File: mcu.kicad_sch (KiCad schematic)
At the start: 4 parts, among them U3 ADAFRUIT_QT_PY

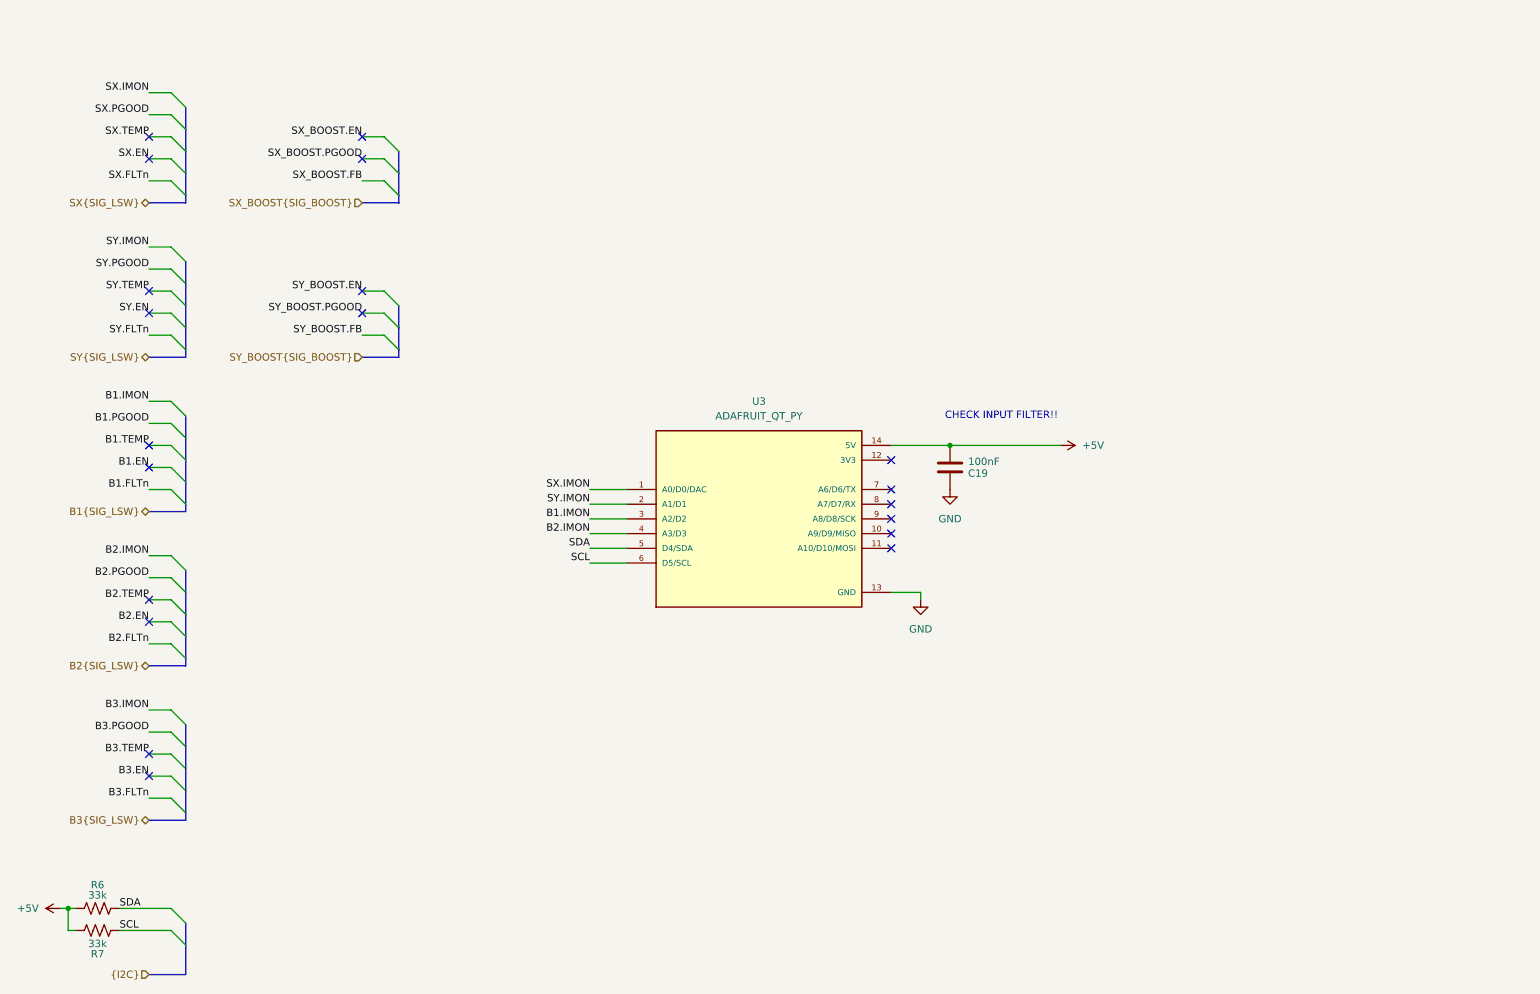
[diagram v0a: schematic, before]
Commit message: imu and load switch for navlight
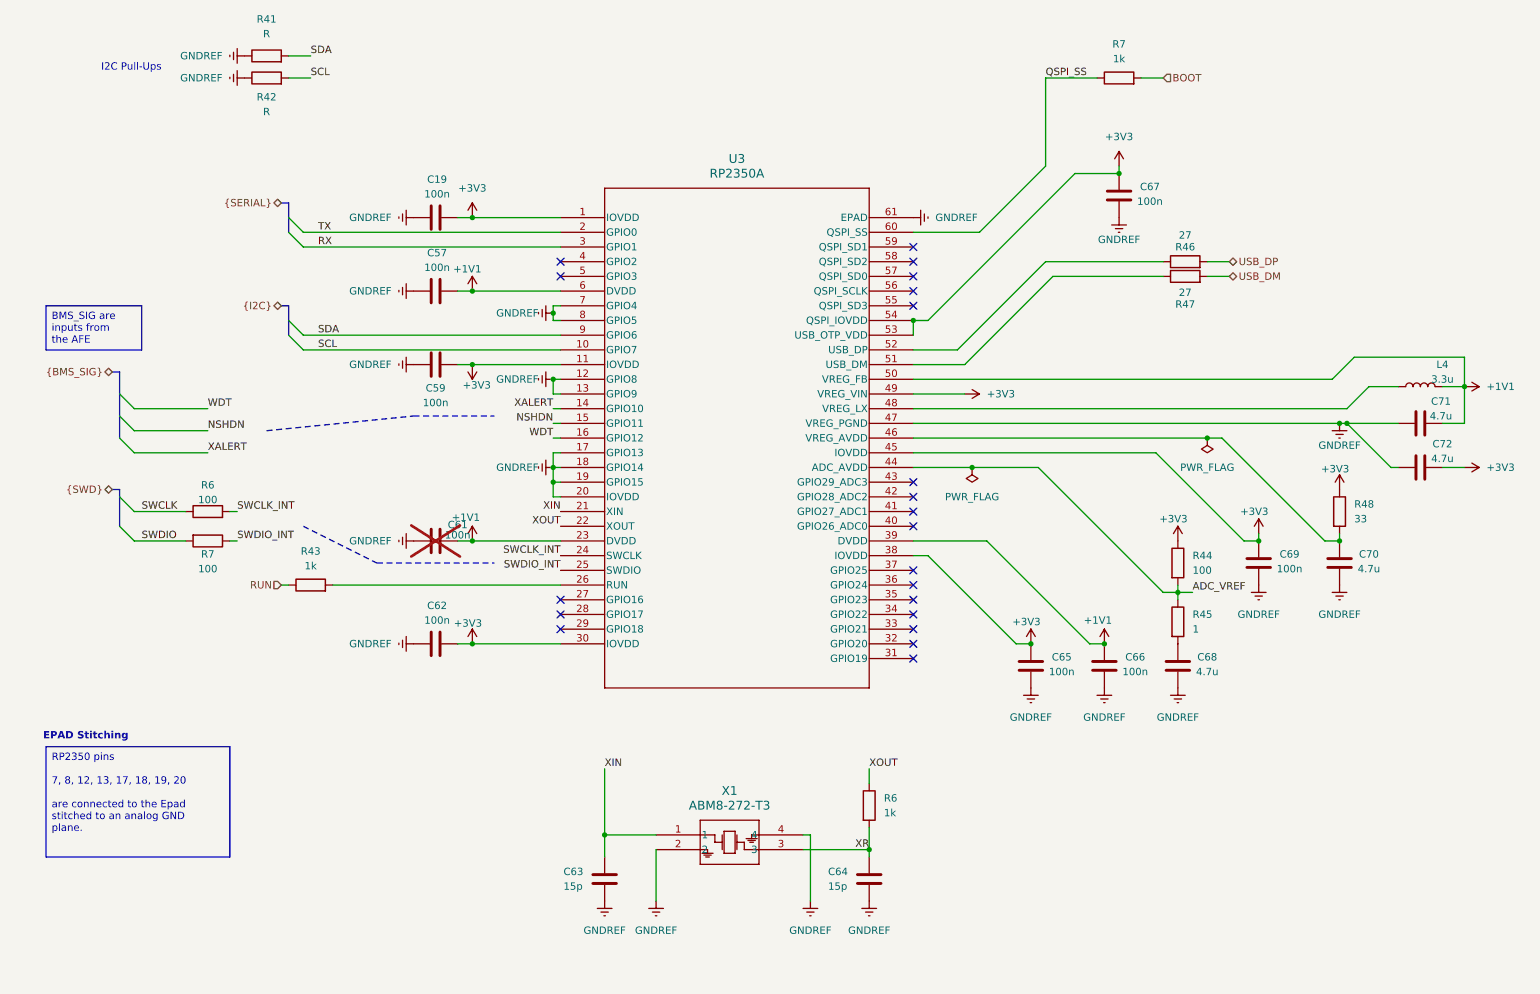
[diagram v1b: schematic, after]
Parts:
- removed R6, R7: 33k, Resistor_SMD:R_0603_1608Metric, symbol Device:R_US
- removed U3: ADAFRUIT_QT_PY, _Power_Board:MODULE_ADAFRUIT_QT_PY, symbol _RP2040:ADAFRUIT_QT_PY
- added C57, C59, C61, C62, C65, C66, C67, C69: 100n, Capacitor_SMD:C_0201_0603Metric, symbol Device:C
- added C63, C64: 15p, Resistor_SMD:R_0201_0603Metric, symbol Device:C
- added C68, C70, C71, C72: 4.7u, Capacitor_SMD:C_0402_1005Metric, symbol Device:C
- added L4: 3.3u, Inductor_SMD:L_0805_2012Metric, symbol Device:L
- added R41, R42: R, symbol Device:R
- added R43, R7: 1k, Resistor_SMD:R_0402_1005Metric, symbol Device:R
- added R44: 100, Capacitor_SMD:C_0402_1005Metric, symbol Device:R
- added R45: 1, Resistor_SMD:R_0402_1005Metric, symbol Device:R
- added R46, R47: 27, Resistor_SMD:R_0201_0603Metric, symbol Device:R
- added R48: 33, Resistor_SMD:R_0402_1005Metric, symbol Device:R
- added R6, R7: 100, Resistor_SMD:R_0201_0603Metric, symbol Device:R
- added R6: 1k, Resistor_SMD:R_0201_0603Metric, symbol Device:R
- added U3: RP2350A, _BMS:QFN-60_7X7_RPI, symbol _RP2354A:RP2350A
- added X1: ABM8-272-T3, _BMS:ABM8-272-T3_ABR, symbol _AMB8:ABM8-272-T3
- C19: value 100nF -> 100n; footprint Capacitor_SMD:C_1206_3216Metric -> Capacitor_SMD:C_0201_0603Metric; Mfr P/N GCM31C5C1H104FA16L -> GRT033R60J104KE01D; Supplier_1 P/N 490-GCM31C5C1H104FA16LTR-ND -> 490-16306-2-ND; Supplier_1 Unit Price 0.98000 -> 0.10000
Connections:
- net SCL: now also R42.2, U3.10 (GPIO7)
- net SDA: now also R41.2, U3.9 (GPIO6)
- net +5V renamed GNDREF
- net GNDREF: now also C57.1, C59.1, C61.1, C62.1, C63.2, C64.2, C65.2, C66.2, C67.2, C68.2, C69.2, C70.2, C71.1, C72.1, R41.1, R42.1, U3.12 (GPIO8), U3.13 (GPIO9), U3.17 (GPIO13), U3.18 (GPIO14), U3.19 (GPIO15), U3.20 (IOVDD), U3.47 (VREG_PGND), U3.61 (EPAD), U3.7 (GPIO4), U3.8 (GPIO5), X1.2, X1.4
- net GND renamed +3V3
- net +3V3: now also C59.2, C62.2, C65.1, C67.1, C69.1, C72.2, R44.1, R48.1, U3.1 (IOVDD), U3.11 (IOVDD), U3.30 (IOVDD), U3.38 (IOVDD), U3.45 (IOVDD), U3.49 (VREG_VIN), U3.53 (USB_OTP_VDD), U3.54 (QSPI_IOVDD)
- new net: L4.1, U3.48 (VREG_LX)
- new net: C68.1, R45.2
- new net: R43.2, U3.26 (RUN)
- new net: C70.1, R48.2, U3.46 (VREG_AVDD)
- new net: R47.1, U3.51 (USB_DM)
- new net: R46.1, U3.52 (USB_DP)
- new net +1V1: C57.2, C61.2, C66.1, C71.2, L4.2, U3.23 (DVDD), U3.39 (DVDD), U3.50 (VREG_FB), U3.6 (DVDD)
- new net ADC_VREF: R44.2, R45.1, U3.44 (ADC_AVDD)
- new net BOOT: R7.2
- new net NSHDN: U3.15 (GPIO11)
- new net QSPI_SS: R7.1, U3.60 (QSPI_SS)
- new net RUN: R43.1
- new net RX: U3.3 (GPIO1)
- new net SWCLK: R6.1
- new net SWCLK_INT: R6.2, U3.24 (SWCLK)
- new net SWDIO: R7.2
- new net SWDIO_INT: R7.1, U3.25 (SWDIO)
- new net TX: U3.2 (GPIO0)
- new net USB_DM: R47.2
- new net USB_DP: R46.2
- new net WDT: U3.16 (GPIO12)
- new net XALERT: U3.14 (GPIO10)
- new net XIN: C63.1, U3.21 (XIN), X1.1
- new net XOUT: R6.1, U3.22 (XOUT)
- new net XR: C64.1, R6.2, X1.3
- no-connect marks 20 -> 21
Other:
- note added: "EPAD Stitching"
- note added: "I2C Pull-Ups"
- note removed: "CHECK INPUT FILTER!!"
- title: House keeping -> IMU

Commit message: PowerBoard update with LVBUS
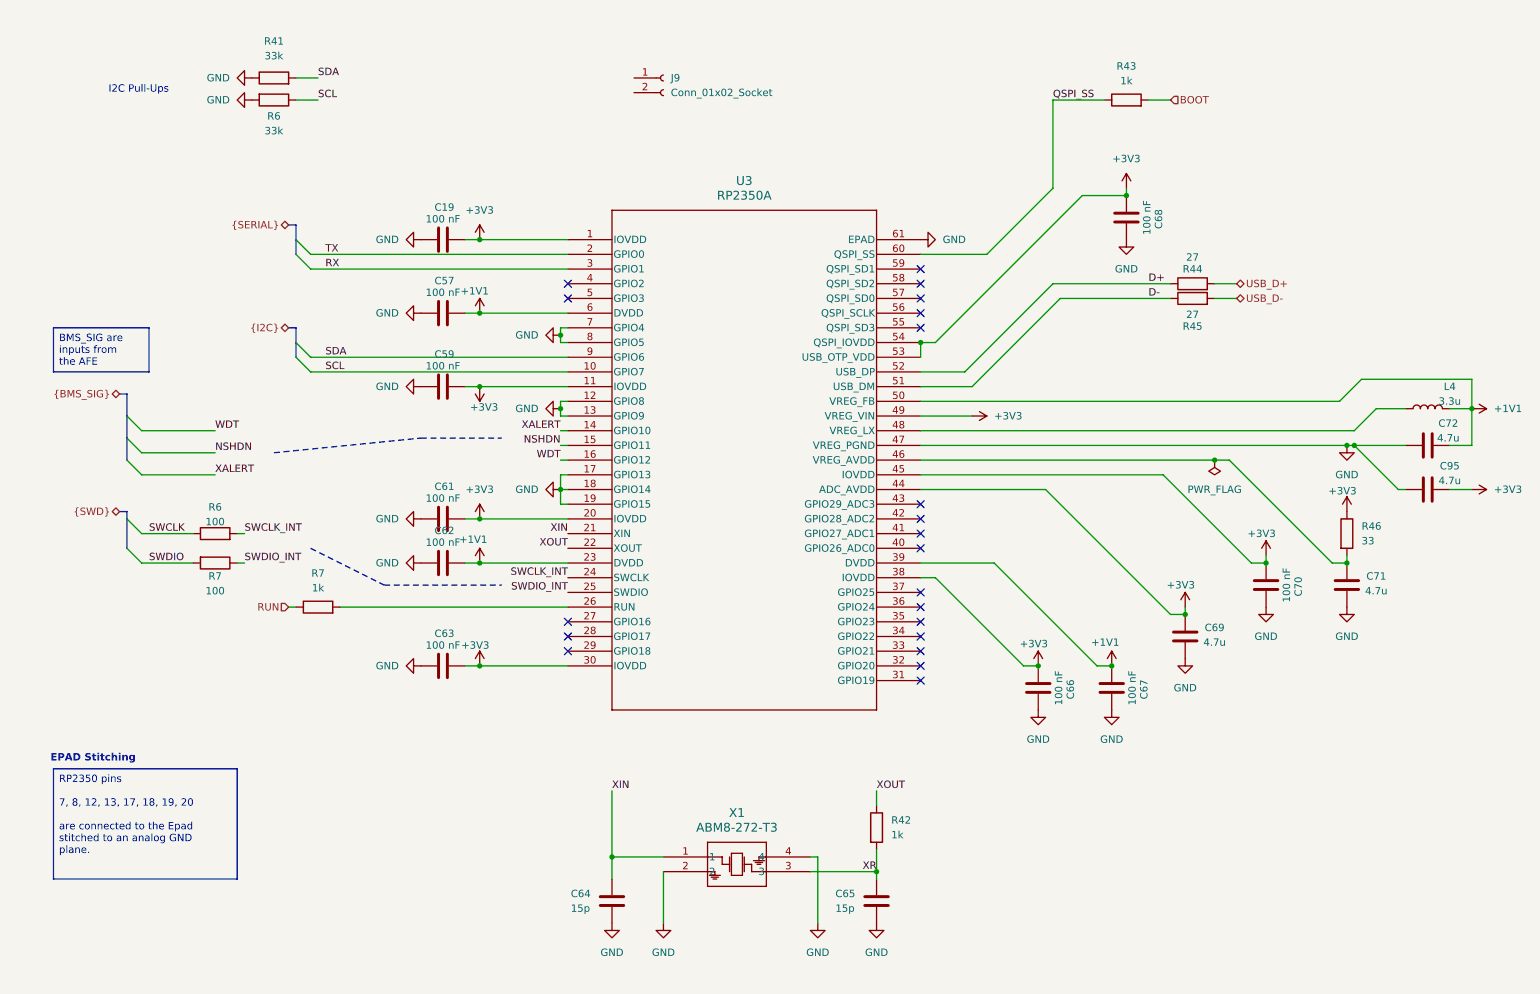
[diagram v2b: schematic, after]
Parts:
- removed R47: 27, Resistor_SMD:R_0201_0603Metric, symbol Device:R
- removed R48: 33, Resistor_SMD:R_0402_1005Metric, symbol Device:R
- removed R6, R7: 100, Resistor_SMD:R_0201_0603Metric, symbol Device:R
- removed R6: 1k, Resistor_SMD:R_0201_0603Metric, symbol Device:R
- removed R7: 1k, Resistor_SMD:R_0402_1005Metric, symbol Device:R
- added C95: 4.7u, Capacitor_SMD:C_0402_1005Metric, symbol Device:C
- added J9: Conn_01x02_Socket, Connector_JST:JST_PH_B2B-PH-K_1x02_P2.00mm_Vertical, symbol Connector:Conn_01x02_Socket
- added R6, R7: 100, Resistor_SMD:R_0201_0603Metric, symbol Device:R
- added R6: 33k, Resistor_SMD:R_0402_1005Metric, symbol Device:R
- added R7: 1k, Resistor_SMD:R_0402_1005Metric, symbol Device:R
- C19, C57, C59, C62, C66, C67: value 100n -> 100 nF; footprint Capacitor_SMD:C_0201_0603Metric -> Capacitor_SMD:C_0402_1005Metric; Mfr P/N GRT033R60J104KE01D -> GRM155C71H104JE19D; Supplier_1 Digikey -> DigiKey; Supplier_1 P/N 490-16306-2-ND -> 490-GRM155C71H104JE19DTR-ND; Supplier_1 Price @ QTY (none) -> 1; Supplier_1 Price @ Qty 1 -> (none)
- C61: value 100n -> 100 nF; footprint Capacitor_SMD:C_0201_0603Metric -> Capacitor_SMD:C_0402_1005Metric; Mfr P/N GRT033R60J104KE01D -> GRM155C71H104JE19D; Supplier_1 Digikey -> DigiKey; Supplier_1 P/N 490-16306-2-ND -> 490-GRM155C71H104JE19DTR-ND; Supplier_1 Price @ QTY (none) -> 1; Supplier_1 Price @ Qty 1 -> (none); now fitted; now in the parts list
- C63: value 15p -> 100 nF; footprint Resistor_SMD:R_0201_0603Metric -> Capacitor_SMD:C_0402_1005Metric; Mfr P/N GRM0335C1E150JA01D -> GRM155C71H104JE19D; Supplier_1 Digikey -> DigiKey; Supplier_1 P/N 490-9658-2-ND -> 490-GRM155C71H104JE19DTR-ND; Supplier_1 Price @ QTY (none) -> 1; Supplier_1 Price @ Qty 1 -> (none)
- C65: value 100n -> 15p; footprint Capacitor_SMD:C_0201_0603Metric -> Resistor_SMD:R_0201_0603Metric; Mfr P/N GRT033R60J104KE01D -> GRM0335C1E150JA01D; Supplier_1 P/N 490-16306-2-ND -> 490-9658-2-ND
- C68, C70: value 4.7u -> 100 nF; Mfr P/N GRM155R60J475ME87D -> GRM155C71H104JE19D; Supplier_1 Digkey -> DigiKey; Supplier_1 P/N 490-5408-2-ND -> 490-GRM155C71H104JE19DTR-ND; Supplier_1 Price @ QTY (none) -> 1; Supplier_1 Price @ Qty 1 -> (none)
- C69: value 100n -> 4.7u; footprint Capacitor_SMD:C_0201_0603Metric -> Capacitor_SMD:C_0402_1005Metric; Mfr P/N GRT033R60J104KE01D -> GRM155R60J475ME87D; Supplier_1 Digikey -> Digkey; Supplier_1 P/N 490-16306-2-ND -> 490-5408-2-ND
- R41: value R -> 33k; footprint (none) -> Resistor_SMD:R_0402_1005Metric; Mfr (none) -> KOA Speer Electronics, Inc.; Mfr P/N (none) -> RN73R1ETTP3302B25; Supplier_1 (none) -> Digikey; Supplier_1 P/N (none) -> 2019-RN73R1ETTP3302B25TR-ND; Supplier_1 Price @ Qty (none) -> 1; Supplier_1 Unit Price (none) -> 0.10000
- R42: value R -> 1k; footprint (none) -> Resistor_SMD:R_0201_0603Metric; Mfr (none) -> Bourns Inc.; Mfr P/N (none) -> CR0201AFW-1001GAS; Supplier_1 (none) -> Digikey; Supplier_1 P/N (none) -> CR0201AFW-1001GASTR-ND; Supplier_1 Price @ Qty (none) -> 1; Supplier_1 Unit Price (none) -> 0.1
- R44: value 100 -> 27; footprint Capacitor_SMD:C_0402_1005Metric -> Resistor_SMD:R_0201_0603Metric; Mfr P/N RC0402FR-07100RL -> RC0201FR-0727RL; Supplier_1 P/N 311-100LRTR-ND -> YAG2554TR-ND
- R45: value 1 -> 27; footprint Resistor_SMD:R_0402_1005Metric -> Resistor_SMD:R_0201_0603Metric; Mfr Stackpole Electronics Inc -> YAGEO; Mfr P/N RMCF0402FT1R00 -> RC0201FR-0727RL; Supplier_1 P/N 738-RMCF0402FT1R00TR-ND -> YAG2554TR-ND
- R46: value 27 -> 33; footprint Resistor_SMD:R_0201_0603Metric -> Resistor_SMD:R_0402_1005Metric; Mfr YAGEO -> Vishay Dale; Mfr P/N RC0201FR-0727RL -> TNPW040233R0DEED; Supplier_1 P/N YAG2554TR-ND -> 541-TNPW040233R0DEEDTR-ND; Supplier_1 Unit Price 0.10000 -> 0.20000
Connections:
- net USB_DP is gone; now on an unnamed net: R46.2
- net +1V1: now also C57.1, C62.1, C67.2, C72.2; no longer C57.2, C61.2, C66.1, C71.2
- net +3V3: now also C19.1, C59.1, C61.1, C63.1, C66.2, C68.2, C70.2, R46.1, U3.20 (IOVDD), U3.44 (ADC_AVDD), C95.2; no longer C19.2, C59.2, C62.2, C65.1, C67.1, C72.2, R44.1
- net BOOT: now also R43.2
- net QSPI_SS: now also R43.1
- net RUN: now also R7.1; no longer R43.1
- net SCL: now also R6.1; no longer R42.2
- net SWCLK: now also R6.1
- net SWCLK_INT: now also R6.2
- net SWDIO: now also R7.2
- net SWDIO_INT: now also R7.1
- net XIN: now also C64.1; no longer C63.1
- net XOUT: now also R42.1
- net XR: now also C65.1, R42.2; no longer C64.1
- net GND: now reaches C68.1
- net GND: now also C19.2, C57.2, C59.2, C61.2, C62.2, C63.2, C64.2, C65.2, C66.1, C67.1, C69.2, C70.1, C71.2, C72.1, R41.1, U3.12 (GPIO8), U3.13 (GPIO9), U3.17 (GPIO13), U3.18 (GPIO14), U3.19 (GPIO15), U3.47 (VREG_PGND), U3.61 (EPAD), U3.7 (GPIO4), U3.8 (GPIO5), X1.2, X1.4, C95.1, R6.2; no longer R45.2
- net at U3.26 (RUN): now also R7.2; no longer R43.2
- net at U3.46 (VREG_AVDD): now also C71.1; no longer C70.1
- net D-: now reaches U3.51 (USB_DM)
- net D-: now also R45.1
- net D+: now reaches U3.52 (USB_DP)
- net D+: now also R44.1; no longer R46.1
- removed net ADC_VREF: R44.2, R45.1, U3.44 (ADC_AVDD)
- removed net GNDREF: C19.1, C57.1, C59.1, C61.1, C62.1, C63.2, C64.2, C65.2, C66.2, C67.2, C68.2, C69.2, C70.2, C71.1, C72.1, R41.1, R42.1, U3.12 (GPIO8), U3.13 (GPIO9), U3.17 (GPIO13), U3.18 (GPIO14), U3.19 (GPIO15), U3.20 (IOVDD), U3.47 (VREG_PGND), U3.61 (EPAD), U3.7 (GPIO4), U3.8 (GPIO5), X1.2, X1.4
- new net USB_D+: R44.2
- new net USB_D-: R45.2
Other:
- moved on the sheet: U3, X1

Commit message: Starting bus load switch layout
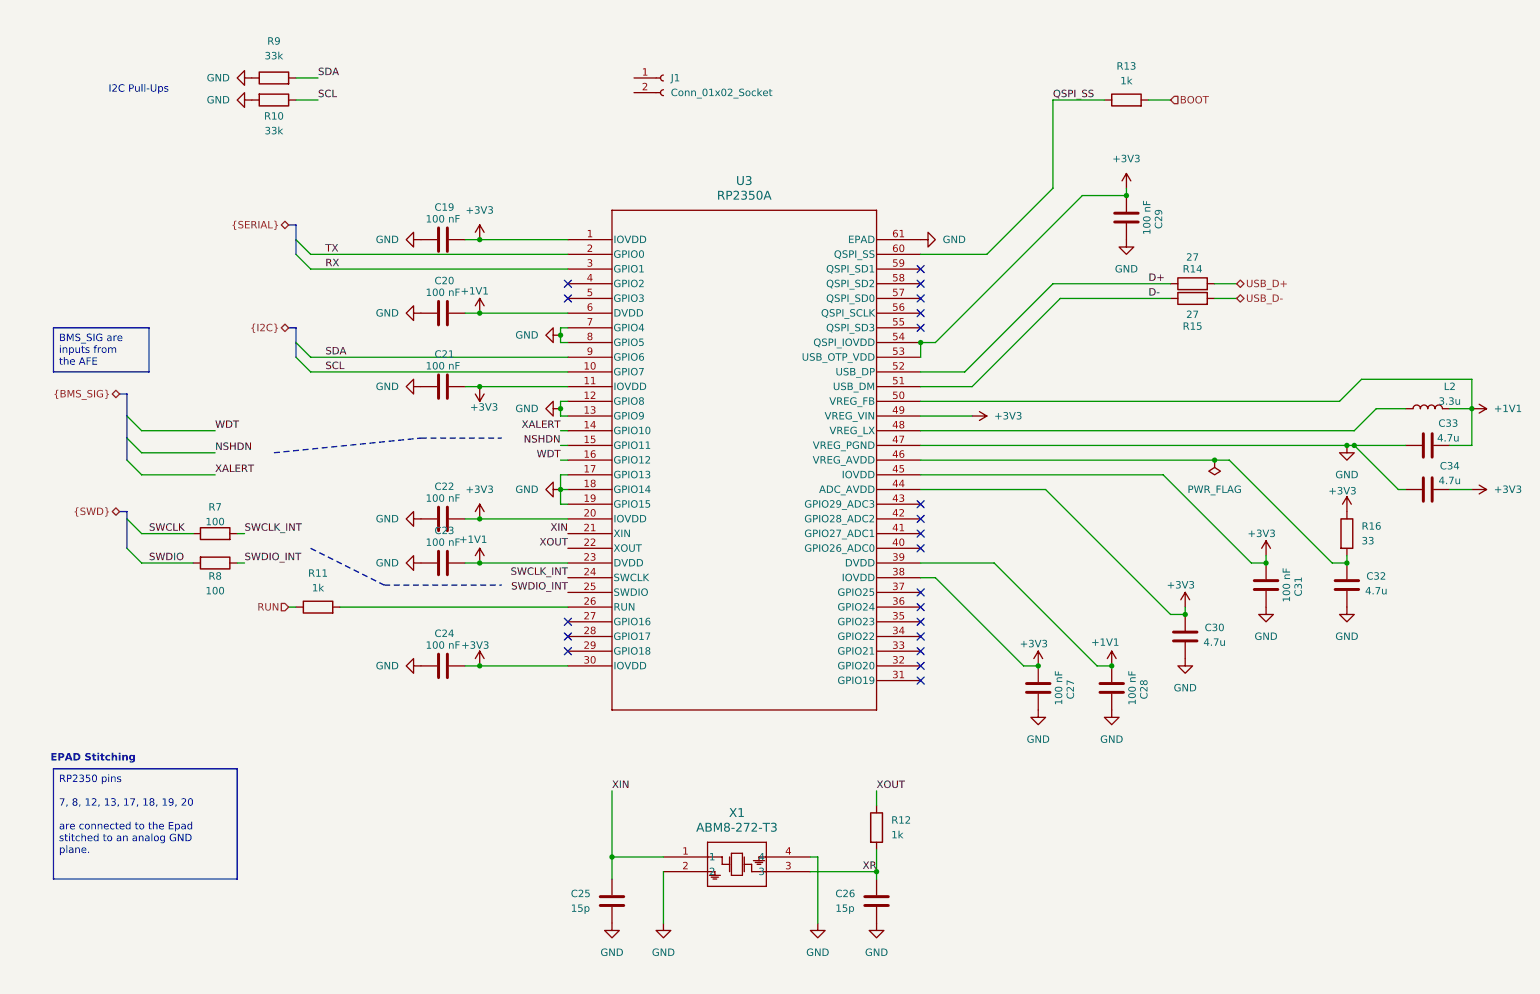
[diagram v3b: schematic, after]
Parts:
- renumbered C57 to C20, C59 to C21, C61 to C22, C62 to C23, C63 to C24, C64 to C25, C65 to C26, C66 to C27, C67 to C28, C68 to C29, C69 to C30, C70 to C31, C71 to C32, C72 to C33, C95 to C34, J9 to J1, L4 to L2, R6 to R10, R7 to R11, R42 to R12, R43 to R13, R44 to R14, R45 to R15, R46 to R16, R6 to R7, R7 to R8, R41 to R9
